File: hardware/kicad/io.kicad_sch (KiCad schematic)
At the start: 13 parts, among them J4 UART_A, J5 UART_B, J6 Port_A, J7 Port_B, U1 74AC04, U11 74AC138, U12 SC16C752, U13 W65C22S

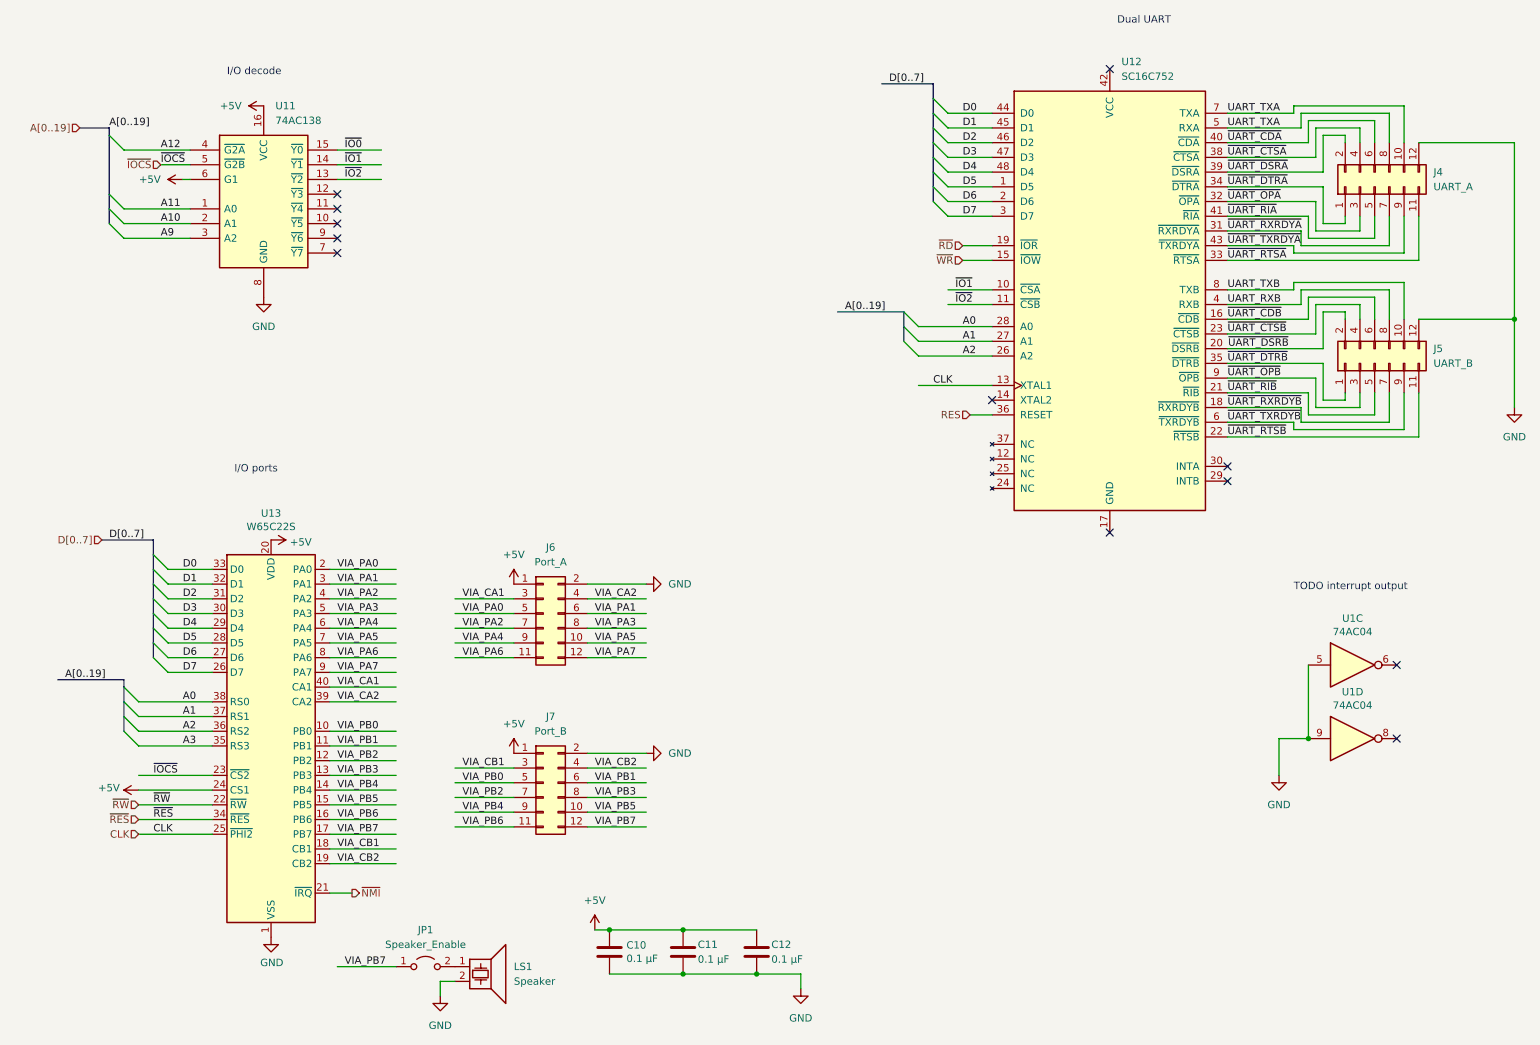
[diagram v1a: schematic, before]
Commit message: update schematic, add draft PCB
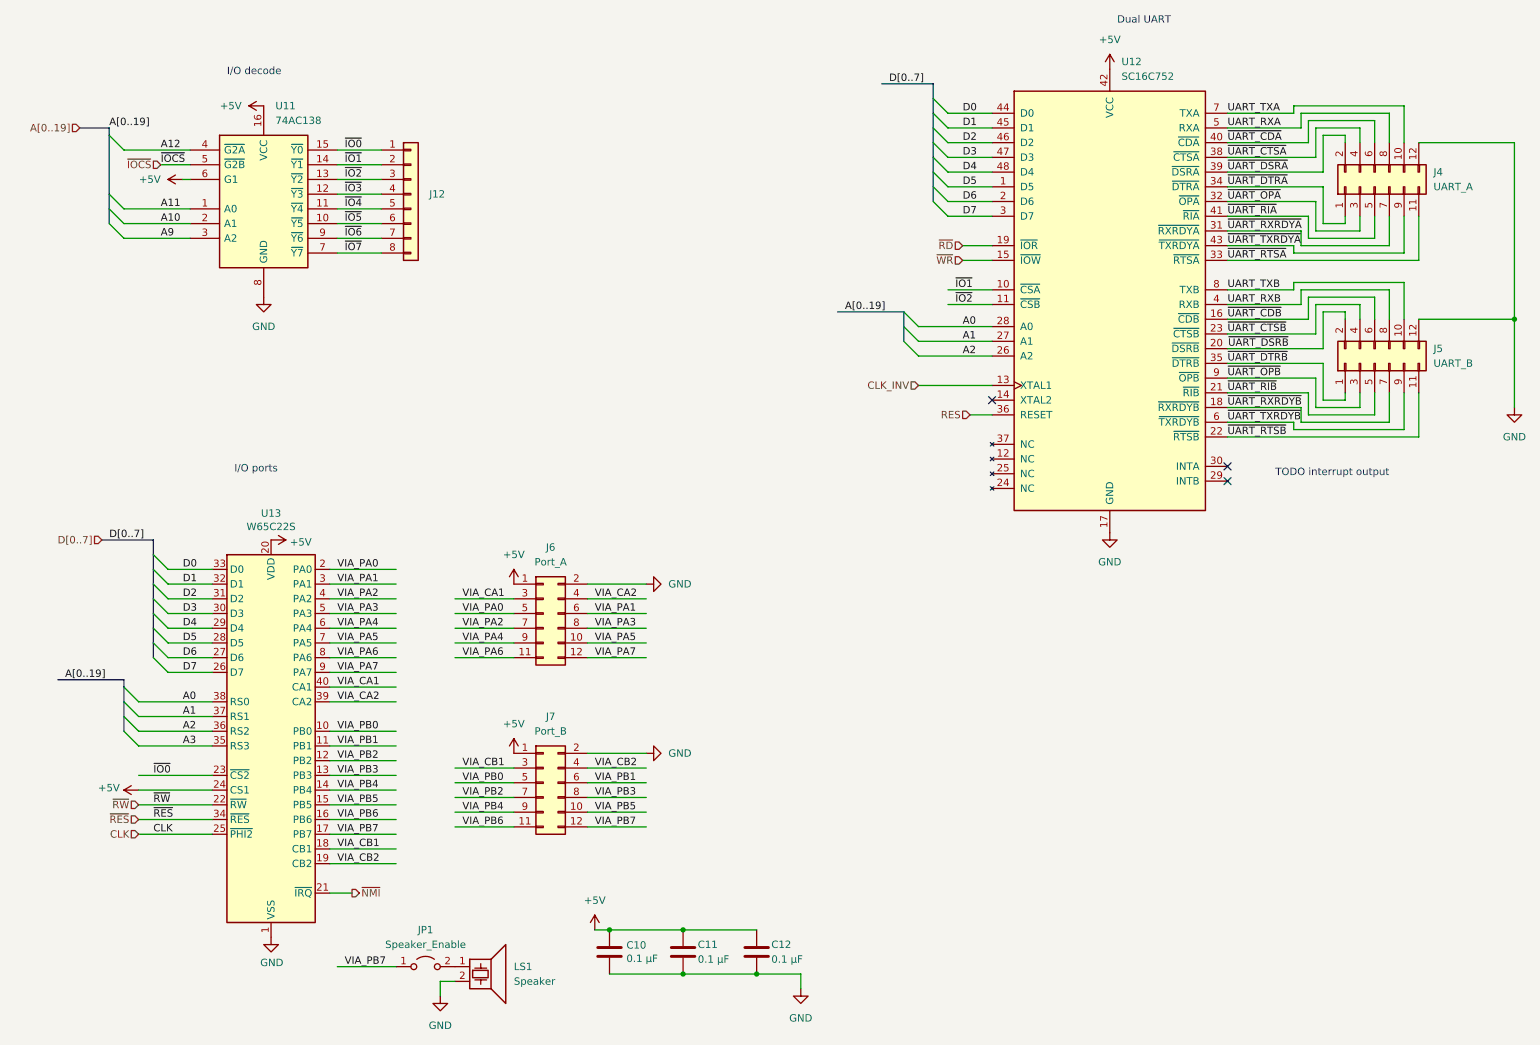
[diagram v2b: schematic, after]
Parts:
- removed U1: 74AC04, Package_DIP:DIP-14_W7.62mm_Socket, symbol project:74AC04
- added J12: (no value), symbol Connector_Generic:Conn_01x08
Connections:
- net +5V: now also U12.42 (VCC)
- net CLK: no longer U12.13 (XTAL1)
- net GND: now also U12.17 (GND)
- net UART_TXA: no longer J4.8 (Pin_8), U12.5 (RXA)
- net ~{IO0}: now also U13.23 (~{CS2}), J12.1 (Pin_1)
- net ~{IO1}: now also J12.2 (Pin_2)
- net ~{IO2}: now also J12.3 (Pin_3)
- net ~{IOCS}: no longer U13.23 (~{CS2})
- net ~{IO5}: now reaches U11.10 (~{Y5})
- net ~{IO5}: now also J12.6 (Pin_6)
- net ~{IO4}: now reaches U11.11 (~{Y4})
- net ~{IO4}: now also J12.5 (Pin_5)
- net ~{IO3}: now reaches U11.12 (~{Y3})
- net ~{IO3}: now also J12.4 (Pin_4)
- net ~{IO7}: now reaches U11.7 (~{Y7})
- net ~{IO7}: now also J12.8 (Pin_8)
- net ~{IO6}: now reaches U11.9 (~{Y6})
- net ~{IO6}: now also J12.7 (Pin_7)
- new net CLK_INV: U12.13 (XTAL1)
- new net UART_RXA: J4.8 (Pin_8), U12.5 (RXA)
- no-connect marks 12 -> 3
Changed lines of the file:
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@@
   (junction (at 273.05 69.85) (diameter 0) (color 0 0 0 0)
   )
-  (junction (at 237.49 142.24) (diameter 0) (color 0 0 0 0)
-  )
   (junction (at 129.54 175.26) (diameter 0) (color 0 0 0 0)
   )
@@
   )
   (no_connect (at 182.88 83.82))
-  (no_connect (at 69.85 48.26))
   (no_connect (at 223.52 97.79))
   (no_connect (at 223.52 95.25))
-  (no_connect (at 252.73 142.24))
-  (no_connect (at 252.73 129.54))
-  (no_connect (at 69.85 58.42))
-  (no_connect (at 69.85 50.8))
-  (no_connect (at 203.2 26.67))
-  (no_connect (at 203.2 106.68))
-  (no_connect (at 69.85 55.88))
-  (no_connect (at 69.85 53.34))
   (bus_entry (at 38.1 118.11) (size 2.54 2.54)
     (stroke (width 0) (type default) (color 0 0 0 0))
@@
     (stroke (width 0) (type default) (color 0 0 0 0))
   )
+  (wire (pts (xy 69.85 50.8) (xy 77.47 50.8))
+    (stroke (width 0) (type default) (color 0 0 0 0))
+  )
   (wire (pts (xy 182.88 39.37) (xy 175.26 39.37))
     (stroke (width 0) (type default) (color 0 0 0 0))
@@
     (stroke (width 0) (type default) (color 0 0 0 0))
   )
-  (wire (pts (xy 232.41 148.59) (xy 232.41 142.24))
-    (stroke (width 0) (type default) (color 0 0 0 0))
-  )
   (wire (pts (xy 35.56 148.59) (xy 48.26 148.59))
     (stroke (width 0) (type default) (color 0 0 0 0))
@@
     (stroke (width 0) (type default) (color 0 0 0 0))
   )
+  (wire (pts (xy 69.85 58.42) (xy 77.47 58.42))
+    (stroke (width 0) (type default) (color 0 0 0 0))
+  )
   (wire (pts (xy 113.03 118.11) (xy 123.19 118.11))
     (stroke (width 0) (type default) (color 0 0 0 0))
@@
     (stroke (width 0) (type default) (color 0 0 0 0))
   )
+  (wire (pts (xy 69.85 53.34) (xy 77.47 53.34))
+    (stroke (width 0) (type default) (color 0 0 0 0))
+  )
   (wire (pts (xy 236.22 87.63) (xy 251.46 87.63))
     (stroke (width 0) (type default) (color 0 0 0 0))
@@
     (stroke (width 0) (type default) (color 0 0 0 0))
   )
+  (wire (pts (xy 69.85 48.26) (xy 77.47 48.26))
+    (stroke (width 0) (type default) (color 0 0 0 0))
+  )
   (wire (pts (xy 238.76 54.61) (xy 246.38 54.61))
     (stroke (width 0) (type default) (color 0 0 0 0))
@@
     (stroke (width 0) (type default) (color 0 0 0 0))
   )
-  (wire (pts (xy 237.49 129.54) (xy 237.49 142.24))
-    (stroke (width 0) (type default) (color 0 0 0 0))
-  )
   (wire (pts (xy 237.49 35.56) (xy 248.92 35.56))
     (stroke (width 0) (type default) (color 0 0 0 0))
@@
     (stroke (width 0) (type default) (color 0 0 0 0))
   )
-  (wire (pts (xy 232.41 142.24) (xy 237.49 142.24))
-    (stroke (width 0) (type default) (color 0 0 0 0))
-  )
   (bus (pts (xy 25.4 36.83) (xy 30.48 36.83))
     (stroke (width 0) (type default) (color 0 0 0 0))
@@
     (stroke (width 0) (type default) (color 0 0 0 0))
   )
+  (wire (pts (xy 69.85 55.88) (xy 77.47 55.88))
+    (stroke (width 0) (type default) (color 0 0 0 0))
+  )
   (wire (pts (xy 90.17 120.65) (xy 100.33 120.65))
     (stroke (width 0) (type default) (color 0 0 0 0))
@@
     (effects (font (size 1.27 1.27)) (justify left bottom))
   )
-  (text "TODO interrupt output" (at 234.95 116.84 0)
+  (text "TODO interrupt output" (at 231.775 97.155 0)
     (effects (font (size 1.27 1.27)) (justify left bottom))
   )
@@
     (effects (font (size 1.27 1.27)) (justify left bottom))
   )
-  (label "CLK" (at 172.72 81.28 0)
-    (effects (font (size 1.27 1.27)) (justify left bottom))
-  )
   (label "D6" (at 177.8 49.53 0)
     (effects (font (size 1.27 1.27)) (justify left bottom))
@@
     (effects (font (size 1.27 1.27)) (justify left bottom))
   )
+  (label "~{IO2}" (at 71.12 45.72 0)
+    (effects (font (size 1.27 1.27)) (justify left bottom))
+  )
+  (label "~{IO3}" (at 71.12 48.26 0)
+    (effects (font (size 1.27 1.27)) (justify left bottom))
+  )
   (label "VIA_PA6" (at 91.44 128.27 0)
     (effects (font (size 1.27 1.27)) (justify left bottom))
@@
     (effects (font (size 1.27 1.27)) (justify left bottom))
   )
-  (label "~{IOCS}" (at 38.1 148.59 0)
+  (label "~{IO0}" (at 38.1 148.59 0)
     (effects (font (size 1.27 1.27)) (justify left bottom))
   )
@@
     (effects (font (size 1.27 1.27)) (justify left bottom))
   )
-  (label "UART_TXA" (at 223.52 36.83 0)
+  (label "UART_RXA" (at 223.52 36.83 0)
     (effects (font (size 1.27 1.27)) (justify left bottom))
   )
@@
     (effects (font (size 1.27 1.27)) (justify left bottom))
   )
+  (label "~{IO4}" (at 71.12 50.8 0)
+    (effects (font (size 1.27 1.27)) (justify left bottom))
+  )
   (label "D2" (at 43.18 118.11 0)
     (effects (font (size 1.27 1.27)) (justify left bottom))
@@
     (effects (font (size 1.27 1.27)) (justify left bottom))
   )
-  (label "~{IO2}" (at 71.12 45.72 0)
-    (effects (font (size 1.27 1.27)) (justify left bottom))
-  )
   (label "A1" (at 177.8 73.66 0)
     (effects (font (size 1.27 1.27)) (justify left bottom))
@@
     (effects (font (size 1.27 1.27)) (justify left bottom))
   )
+  (label "~{IO7}" (at 71.12 58.42 0)
+    (effects (font (size 1.27 1.27)) (justify left bottom))
+  )
   (label "D4" (at 43.18 123.19 0)
     (effects (font (size 1.27 1.27)) (justify left bottom))
@@
     (effects (font (size 1.27 1.27)) (justify left bottom))
   )
+  (label "~{IO6}" (at 71.12 55.88 0)
+    (effects (font (size 1.27 1.27)) (justify left bottom))
+  )
   (label "VIA_PA0" (at 91.44 120.65 0)
     (effects (font (size 1.27 1.27)) (justify left bottom))
@@
   )
   (label "~{UART_CTSB}" (at 223.52 72.39 0)
+    (effects (font (size 1.27 1.27)) (justify left bottom))
+  )
+  (label "~{IO5}" (at 71.12 53.34 0)
     (effects (font (size 1.27 1.27)) (justify left bottom))
   )
@@
   )
   (hierarchical_label "~{WR}" (shape input) (at 177.8 59.69 180)
+    (effects (font (size 1.27 1.27)) (justify right))
+  )
+  (hierarchical_label "CLK_INV" (shape input) (at 170.18 81.28 180)
     (effects (font (size 1.27 1.27)) (justify right))
   )
@@
     (pin "9")
   )
-  (symbol (lib_id "power:GND") (at 232.41 148.59 0) (unit 1)
-    (in_bom yes) (on_board yes) (fields_autoplaced)
-    (property "Reference" "#PWR047" (id 0) (at 232.41 154.94 0)
-      (effects (font (size 1.27 1.27)) hide)
-    )
-    (property "Value" "GND" (id 1) (at 232.41 153.67 0))
-    (property "Footprint" "" (id 2) (at 232.41 148.59 0)
-      (effects (font (size 1.27 1.27)) hide)
-    )
-    (property "Datasheet" "" (id 3) (at 232.41 148.59 0)
-      (effects (font (size 1.27 1.27)) hide)
-    )
-    (pin "1")
-  )
   (symbol (lib_id "power:GND") (at 273.05 85.09 0) (unit 1)
     (in_bom yes) (on_board yes) (fields_autoplaced)
@@
     )
     (pin "1")
-  )
-  (symbol (lib_id "project:74AC04") (at 245.11 142.24 0) (unit 4)
-    (in_bom yes) (on_board yes)
-    (property "Reference" "U1" (id 0) (at 245.11 134.1882 0))
-    (property "Value" "74AC04" (id 1) (at 245.11 136.4996 0))
-    (property "Footprint" "Package_DIP:DIP-14_W7.62mm_Socket" (id 2) (at 245.11 142.24 0)
-      (effects (font (size 1.27 1.27)) hide)
-    )
-    (property "Datasheet" "http://www.ti.com/lit/gpn/sn74LS04" (id 3) (at 245.11 142.24 0)
-      (effects (font (size 1.27 1.27)) hide)
-    )
-    (pin "8")
-    (pin "9")
   )
   (symbol (lib_id "Connector_Generic:Conn_02x06_Odd_Even") (at 248.92 77.47 90) (unit 1)
@@
     (pin "8")
     (pin "9")
+  )
+  (symbol (lib_id "Connector_Generic:Conn_01x08") (at 82.55 48.26 0) (unit 1)
+    (in_bom yes) (on_board yes)
+    (property "Reference" "J12" (id 0) (at 85.725 48.2599 0)
+      (effects (font (size 1.27 1.27)) (justify left))
+    )
+    (property "Value" "" (id 1) (at 85.725 50.7999 0)
+      (effects (font (size 1.27 1.27)) (justify left))
+    )
+    (property "Footprint" "" (id 2) (at 82.55 48.26 0)
+      (effects (font (size 1.27 1.27)) hide)
+    )
+    (property "Datasheet" "~" (id 3) (at 82.55 48.26 0)
+      (effects (font (size 1.27 1.27)) hide)
+    )
+    (pin "1")
+    (pin "2")
+    (pin "3")
+    (pin "4")
+    (pin "5")
+    (pin "6")
+    (pin "7")
+    (pin "8")
   )
   (symbol (lib_id "power:GND") (at 123.19 115.57 90) (unit 1)
@@
     (pin "9")
   )
-  (symbol (lib_id "project:74AC04") (at 245.11 129.54 0) (unit 3)
-    (in_bom yes) (on_board yes)
-    (property "Reference" "U1" (id 0) (at 245.11 121.4882 0))
-    (property "Value" "74AC04" (id 1) (at 245.11 123.7996 0))
-    (property "Footprint" "Package_DIP:DIP-14_W7.62mm_Socket" (id 2) (at 245.11 129.54 0)
-      (effects (font (size 1.27 1.27)) hide)
-    )
-    (property "Datasheet" "http://www.ti.com/lit/gpn/sn74LS04" (id 3) (at 245.11 129.54 0)
-      (effects (font (size 1.27 1.27)) hide)
-    )
-    (pin "5")
-    (pin "6")
-  )
   (symbol (lib_id "power:+5V") (at 114.3 175.26 0) (unit 1)
     (in_bom yes) (on_board yes) (fields_autoplaced)
@@
     (pin "1")
   )
+  (symbol (lib_id "power:+5V") (at 203.2 26.67 0) (unit 1)
+    (in_bom yes) (on_board yes) (fields_autoplaced)
+    (property "Reference" "#PWR0109" (id 0) (at 203.2 30.48 0)
+      (effects (font (size 1.27 1.27)) hide)
+    )
+    (property "Value" "+5V" (id 1) (at 203.2 21.59 0))
+    (property "Footprint" "" (id 2) (at 203.2 26.67 0)
+      (effects (font (size 1.27 1.27)) hide)
+    )
+    (property "Datasheet" "" (id 3) (at 203.2 26.67 0)
+      (effects (font (size 1.27 1.27)) hide)
+    )
+    (pin "1")
+  )
   (symbol (lib_id "Jumper:Jumper_2_Open") (at 85.09 181.61 0) (unit 1)
     (in_bom yes) (on_board yes) (fields_autoplaced)
@@
     (pin "2")
   )
+  (symbol (lib_id "power:GND") (at 203.2 106.68 0) (unit 1)
+    (in_bom yes) (on_board yes) (fields_autoplaced)
+    (property "Reference" "#PWR0108" (id 0) (at 203.2 113.03 0)
+      (effects (font (size 1.27 1.27)) hide)
+    )
+    (property "Value" "GND" (id 1) (at 203.2 111.76 0))
+    (property "Footprint" "" (id 2) (at 203.2 106.68 0)
+      (effects (font (size 1.27 1.27)) hide)
+    )
+    (property "Datasheet" "" (id 3) (at 203.2 106.68 0)
+      (effects (font (size 1.27 1.27)) hide)
+    )
+    (pin "1")
+  )
   (symbol (lib_id "Device:C") (at 129.54 179.07 0) (unit 1)

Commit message: pcb updates
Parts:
- added C16: 4.7 µF, Capacitor_THT:CP_Radial_D4.0mm_P1.50mm, symbol Device:C_Polarized
- added J15: Conn_01x02, Connector_PinHeader_2.54mm:PinHeader_1x02_P2.54mm_Vertical, symbol Connector_Generic:Conn_01x02
- added J18: Conn_01x07, Connector_PinSocket_2.54mm:PinSocket_1x07_P2.54mm_Vertical, symbol Connector_Generic:Conn_01x07
- added J19: (no value), symbol Connector_Generic:Conn_02x03_Odd_Even
- added J20: (no value), symbol Connector_Generic:Conn_01x02
- J12: value (none) -> Conn_01x08; footprint (none) -> Connector_PinHeader_2.54mm:PinHeader_1x08_P2.54mm_Vertical
- U13: footprint Package_DIP:DIP-40_W15.24mm -> Package_DIP:DIP-40_W15.24mm_Socket
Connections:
- net +5V: now also C16.1, J18.7 (Pin_7), J19.1 (Pin_1), J19.3 (Pin_3), J19.5 (Pin_5)
- net GND: now also C16.2, J18.1 (Pin_1), J19.2 (Pin_2), J19.4 (Pin_4), J19.6 (Pin_6), J20.1 (Pin_1), J20.2 (Pin_2)
- net VIA_PA0: now also J18.3 (Pin_3)
- net VIA_PA1: now also J18.4 (Pin_4)
- net VIA_PA2: now also J18.5 (Pin_5)
- net VIA_PA3: now also J18.6 (Pin_6)
- net UART_INTB: now reaches U12.29 (INTB)
- net UART_INTB: now also J15.2 (Pin_2)
- net UART_INTA: now reaches U12.30 (INTA)
- net UART_INTA: now also J15.1 (Pin_1)
- net SPEAKER: now reaches JP1.2 (B), LS1.1
- no-connect marks 3 -> 2
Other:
- note added: "Header for SD card module DEV-13743"
- note added: "Interrupt output to pin header"
- note added: "Power/ground headers"
- note removed: "TODO interrupt output"
- moved on the sheet: LS1
